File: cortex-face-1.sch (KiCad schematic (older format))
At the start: 170 parts, among them J1 Conn_01x04, SW1 SW_Push, U1 Elite-C

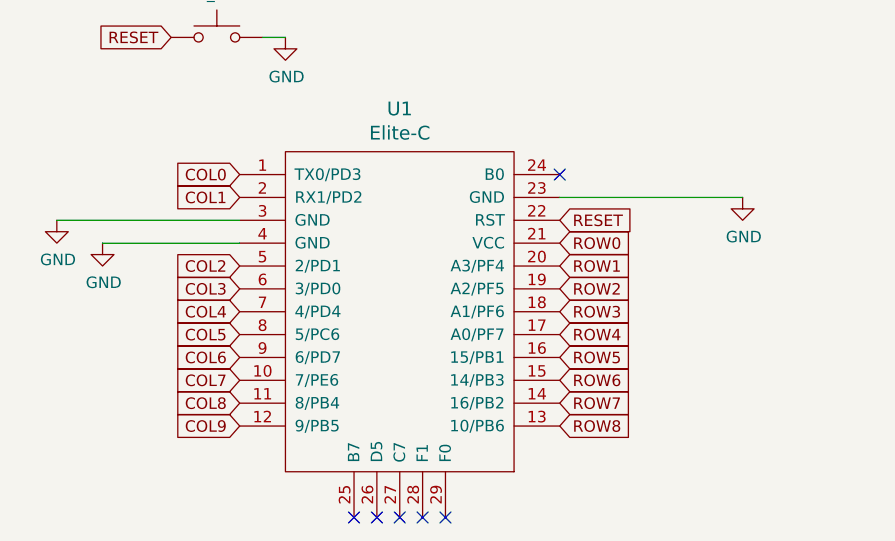
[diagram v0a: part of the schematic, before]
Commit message: Fixed 5V power to Elite-C
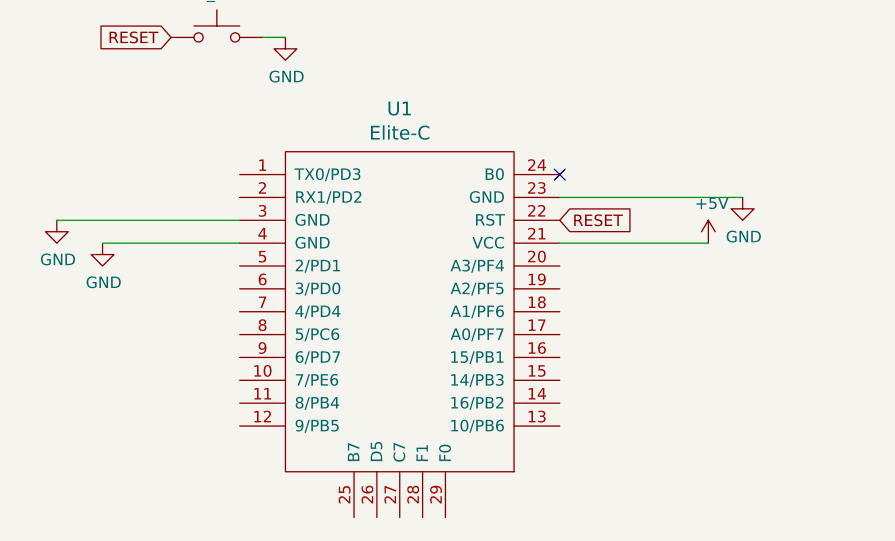
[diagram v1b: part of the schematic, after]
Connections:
- net COL0: no longer U1.1 (TX0/PD3)
- net COL1: no longer U1.2 (RX1/PD2)
- net COL2: no longer U1.5 (2/PD1)
- net COL3: no longer U1.6 (3/PD0)
- net COL4: no longer U1.7 (4/PD4)
- net COL5: no longer U1.8 (5/PC6)
- net COL6: no longer U1.9 (6/PD7)
- net COL7: no longer U1.10 (7/PE6)
- net COL8: no longer U1.11 (8/PB4)
- net COL9: no longer U1.12 (9/PB5)
- net ROW0: no longer U1.21 (VCC)
- net ROW1: no longer U1.20 (A3/PF4)
- net ROW2: no longer U1.19 (A2/PF5)
- net ROW3: no longer U1.18 (A1/PF6)
- net ROW4: no longer U1.17 (A0/PF7)
- net ROW5: no longer U1.16 (15/PB1)
- net ROW6: no longer U1.15 (14/PB3)
- net ROW7: no longer U1.14 (16/PB2)
- net ROW8: no longer U1.13 (10/PB6)
- new net +5V: U1.21 (VCC)
- no-connect marks 6 -> 1
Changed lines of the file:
@@
 $EndComp
 NoConn ~ 3200 5600
-Text GLabel 3200 5900 2    50   Input ~ 0
-ROW0
 $Comp
 L power:GND #PWR0102
@@
 Wire Wire Line
 	1200 5900 1800 5900
-Text GLabel 3200 6100 2    50   Input ~ 0
-ROW2
-Text GLabel 3200 6200 2    50   Input ~ 0
-ROW3
-Text GLabel 3200 6300 2    50   Input ~ 0
-ROW4
-Text GLabel 3200 6400 2    50   Input ~ 0
-ROW5
-Text GLabel 3200 6500 2    50   Input ~ 0
-ROW6
 Text GLabel 3200 5800 2    50   Input ~ 0
 RESET
-Text GLabel 3200 6600 2    50   Input ~ 0
-ROW7
-Text GLabel 3200 6700 2    50   Input ~ 0
-ROW8
 $Comp
 L power:GND #PWR0104
@@
 Wire Wire Line
 	4000 5700 3200 5700
-Text GLabel 3200 6000 2    50   Input ~ 0
-ROW1
-Text GLabel 1800 5600 0    50   Input ~ 0
-COL0
-Text GLabel 1800 5700 0    50   Input ~ 0
-COL1
-Text GLabel 1800 6000 0    50   Input ~ 0
-COL2
-Text GLabel 1800 6100 0    50   Input ~ 0
-COL3
-Text GLabel 1800 6200 0    50   Input ~ 0
-COL4
-Text GLabel 1800 6300 0    50   Input ~ 0
-COL5
-Text GLabel 1800 6400 0    50   Input ~ 0
-COL6
-Text GLabel 1800 6500 0    50   Input ~ 0
-COL7
-Text GLabel 1800 6600 0    50   Input ~ 0
-COL8
-Text GLabel 1800 6700 0    50   Input ~ 0
-COL9
-NoConn ~ 2300 7100
-NoConn ~ 2400 7100
-NoConn ~ 2500 7100
-NoConn ~ 2600 7100
-NoConn ~ 2700 7100
 $Comp
 L MX_Alps_Hybrid:MX-NoLED MX_RALT1
@@
 	0    -1   -1   0
 $EndComp
+$Comp
+L power:+5V #PWR?
+U 1 1 5DFD83F1
+P 3850 5900
+F 0 "#PWR?" H 3850 5750 50  0001 C CNN
+F 1 "+5V" H 3865 6073 50  0000 C CNN
+F 2 "" H 3850 5900 50  0001 C CNN
+F 3 "" H 3850 5900 50  0001 C CNN
+	1    3850 5900
+	1    0    0    -1
+$EndComp
+Wire Wire Line
+	3850 5900 3200 5900
 $EndSCHEMATC

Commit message: First pass at routing
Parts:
- added H1, H10, H2, H3, H4, H5, H6, H7, H8, H9: Hole, MountingHole:MountingHole_6mm, symbol keebio:Hole
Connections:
- net COL0: now also U1.20 (A3/PF4)
- net COL1: now also U1.29 (F0)
- net COL2: now also U1.19 (A2/PF5)
- net COL3: now also U1.14 (16/PB2)
- net COL4: now also U1.5 (2/PD1)
- net COL5: now also U1.25 (B7)
- net COL6: now also U1.12 (9/PB5)
- net COL7: now also U1.11 (8/PB4)
- net COL8: now also U1.10 (7/PE6)
- net COL9: now also U1.13 (10/PB6)
- net ROW0: now also U1.15 (14/PB3)
- net ROW1: now also U1.16 (15/PB1)
- net ROW2: now also U1.17 (A0/PF7)
- net ROW3: now also U1.18 (A1/PF6)
- net ROW4: now also U1.28 (F1)
- net ROW5: now also U1.27 (C7)
- net ROW6: now also U1.9 (6/PD7)
- net ROW7: now also U1.8 (5/PC6)
- net ROW8: now also U1.7 (4/PD4)
- no-connect marks 1 -> 5

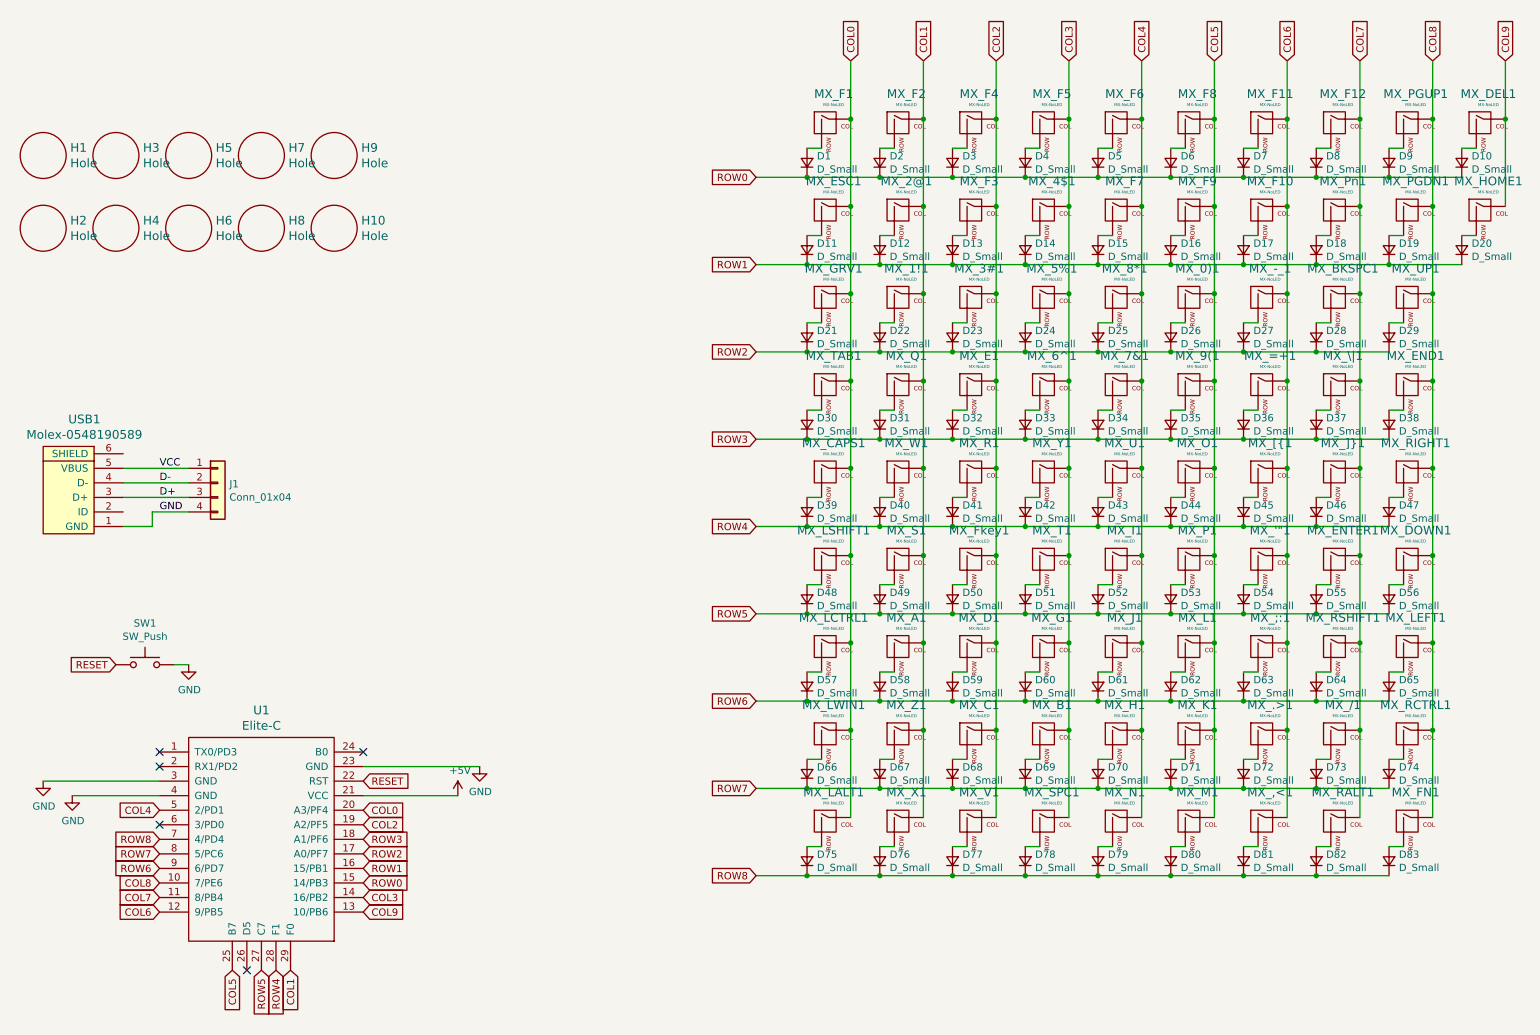
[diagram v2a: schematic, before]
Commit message: Autorouted
Using FreeRouting
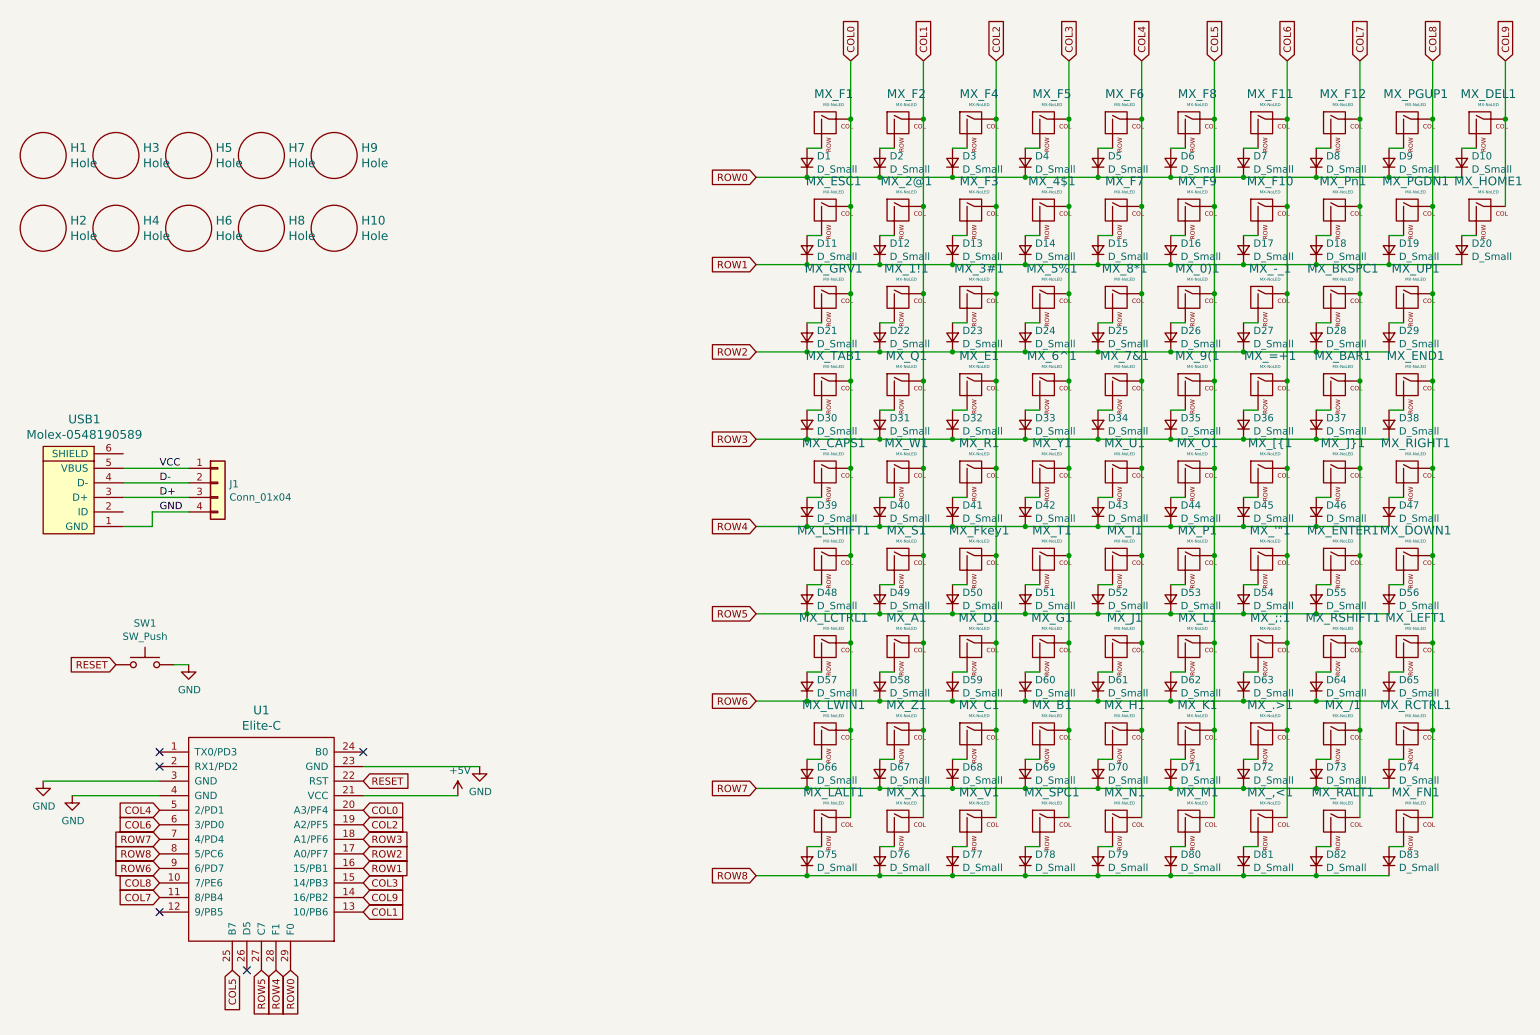
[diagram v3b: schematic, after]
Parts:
- renumbered MX_\|1 to MX_BAR1
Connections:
- net COL1: now also U1.13 (10/PB6); no longer U1.29 (F0)
- net COL3: now also U1.15 (14/PB3); no longer U1.14 (16/PB2)
- net COL6: now also U1.6 (3/PD0); no longer U1.12 (9/PB5)
- net COL9: now also U1.14 (16/PB2); no longer U1.13 (10/PB6)
- net ROW0: now also U1.29 (F0); no longer U1.15 (14/PB3)
- net ROW7: now also U1.7 (4/PD4); no longer U1.8 (5/PC6)
- net ROW8: now also U1.8 (5/PC6); no longer U1.7 (4/PD4)
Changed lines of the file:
@@
 $EndComp
 $Comp
-L MX_Alps_Hybrid:MX-NoLED MX_\|1
+L MX_Alps_Hybrid:MX-NoLED MX_BAR1
 U 1 1 5E0609E8
 P 9900 3100
-F 0 "MX_\\|1" H 9933 3323 60  0000 C CNN
+F 0 "MX_BAR1" H 9933 3323 60  0000 C CNN
 F 1 "MX-NoLED" H 9933 3249 20  0000 C CNN
 F 2 "MX_Only:MXOnly-1.5U-NoLED" H 9275 3075 60  0001 C CNN
@@
 Text GLabel 3200 6000 2    50   Input ~ 0
 COL0
-Text GLabel 2700 7100 3    50   Input ~ 0
+Text GLabel 3200 6700 2    50   Input ~ 0
 COL1
 Text GLabel 3200 6100 2    50   Input ~ 0
 COL2
-Text GLabel 3200 6600 2    50   Input ~ 0
+Text GLabel 3200 6500 2    50   Input ~ 0
 COL3
 Text GLabel 1800 6000 0    50   Input ~ 0
@@
 Text GLabel 2300 7100 3    50   Input ~ 0
 COL5
-Text GLabel 1800 6700 0    50   Input ~ 0
+Text GLabel 1800 6100 0    50   Input ~ 0
 COL6
 Text GLabel 1800 6600 0    50   Input ~ 0
@@
 Text GLabel 1800 6500 0    50   Input ~ 0
 COL8
-Text GLabel 3200 6700 2    50   Input ~ 0
+Text GLabel 3200 6600 2    50   Input ~ 0
 COL9
-Text GLabel 3200 6500 2    50   Input ~ 0
+Text GLabel 2700 7100 3    50   Input ~ 0
 ROW0
 Text GLabel 3200 6400 2    50   Input ~ 0
@@
 Text GLabel 1800 6400 0    50   Input ~ 0
 ROW6
+Text GLabel 1800 6200 0    50   Input ~ 0
+ROW7
 Text GLabel 1800 6300 0    50   Input ~ 0
-ROW7
-Text GLabel 1800 6200 0    50   Input ~ 0
 ROW8
 NoConn ~ 1800 5600
 NoConn ~ 1800 5700
-NoConn ~ 1800 6100
 NoConn ~ 2400 7100
+NoConn ~ 1800 6700
 $EndSCHEMATC
